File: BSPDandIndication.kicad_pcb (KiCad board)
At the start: 2 copper layers, 50 parts, among them J1 Power12, J2 Masa, J3 12VTelem, J4 Sensors, J5 12VTelem, J6 BSPD12OUT, K1 FINDER-36.11, Q1 BC817, U1 LM1117-5.0, U2 LM1117-5.0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

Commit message: Update J5 value
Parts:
- J5: value 12VTelem -> LED
- moved J4 101.0 mm to (63.5, 137.1), turned to 180 degrees
- moved J2 85.6 mm to (25.4, 132.1), turned to 90 degrees
- moved J3 59.3 mm to (25.4, 119.4), turned to 90 degrees
- moved J5 54.5 mm to (73.7, 101.6)
- moved J1 42.6 mm to (25.4, 106.7), turned to 90 degrees
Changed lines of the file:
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@@
   )
   (footprint "AK3001:AK300_1x02_P5.00mm_45-Degree" (layer "F.Cu")
-    (at 58.775 49.215)
+    (at 73.66 101.6)
     (descr "AK3001 serie terminal block")
     (tags "AK3001 serie connector")
@@
       (effects (font (size 1 1) (thickness 0.15)))
     )
-    (fp_text value "12VTelem" (at 2.5 11) (layer "F.Fab")
+    (fp_text value "LED" (at 2.5 11) (layer "F.Fab")
       (effects (font (size 1 1) (thickness 0.15)))
     )
@@
   )
   (footprint "AK3001:AK3001_1x04_P5.00mm_45-Degree" (layer "F.Cu")
-    (at 25.085 43.615)
+    (at 63.45 137.08 180)
     (descr "AK3001 serie terminal block")
     (tags "AK3001 serie connector")
@@
     (fp_line (start 17.53 8.636) (end -2.47 8.636) (layer "F.Fab") (width 0.1))
     (fp_line (start -2.47 8.636) (end -2.47 -5.5) (layer "F.Fab") (width 0.1))
-    (pad "1" thru_hole rect (at 0.03 5) (size 3 3) (drill 1.5) (layers *.Cu *.Mask)
+    (pad "1" thru_hole rect (at 0.03 5 180) (size 3 3) (drill 1.5) (layers *.Cu *.Mask)
       (net 2 "GND") (pinfunction "Pin_1") (pintype "passive"))
-    (pad "1" thru_hole rect (at 0.03 0) (size 3 3) (drill 1.5) (layers *.Cu *.Mask)
+    (pad "1" thru_hole rect (at 0.03 0 180) (size 3 3) (drill 1.5) (layers *.Cu *.Mask)
       (net 2 "GND") (pinfunction "Pin_1") (pintype "passive"))
-    (pad "2" thru_hole circle (at 5.03 5) (size 3 3) (drill 1.5) (layers *.Cu *.Mask)
+    (pad "2" thru_hole circle (at 5.03 5 180) (size 3 3) (drill 1.5) (layers *.Cu *.Mask)
       (net 16 "Brake2") (pinfunction "Pin_2") (pintype "passive"))
-    (pad "2" thru_hole circle (at 5.03 0) (size 3 3) (drill 1.5) (layers *.Cu *.Mask)
+    (pad "2" thru_hole circle (at 5.03 0 180) (size 3 3) (drill 1.5) (layers *.Cu *.Mask)
       (net 16 "Brake2") (pinfunction "Pin_2") (pintype "passive"))
-    (pad "3" thru_hole circle (at 10.03 0) (size 3 3) (drill 1.5) (layers *.Cu *.Mask)
+    (pad "3" thru_hole circle (at 10.03 0 180) (size 3 3) (drill 1.5) (layers *.Cu *.Mask)
       (net 17 "Brake1") (pinfunction "Pin_3") (pintype "passive"))
-    (pad "3" thru_hole circle (at 10.03 5) (size 3 3) (drill 1.5) (layers *.Cu *.Mask)
+    (pad "3" thru_hole circle (at 10.03 5 180) (size 3 3) (drill 1.5) (layers *.Cu *.Mask)
       (net 17 "Brake1") (pinfunction "Pin_3") (pintype "passive"))
-    (pad "4" thru_hole circle (at 15.03 5) (size 3 3) (drill 1.5) (layers *.Cu *.Mask)
+    (pad "4" thru_hole circle (at 15.03 5 180) (size 3 3) (drill 1.5) (layers *.Cu *.Mask)
       (net 18 "TPS") (pinfunction "Pin_4") (pintype "passive"))
-    (pad "4" thru_hole circle (at 15.03 0) (size 3 3) (drill 1.5) (layers *.Cu *.Mask)
+    (pad "4" thru_hole circle (at 15.03 0 180) (size 3 3) (drill 1.5) (layers *.Cu *.Mask)
       (net 18 "TPS") (pinfunction "Pin_4") (pintype "passive"))
     (model "${KICAD6_3DMODEL_DIR}/TerminalBlock_Altech.3dshapes/Altech_AK300_1x04_P5.00mm_45-Degree.wrl"
@@
   )
   (footprint "AK3001:AK300_1x02_P5.00mm_45-Degree" (layer "F.Cu")
-    (at 25.115 60.085)
+    (at 25.4 119.38 90)
     (descr "AK3001 serie terminal block")
     (tags "AK3001 serie connector")
@@
     (property "Sheetname" "")
     (attr through_hole)
-    (fp_text reference "J3" (at 0 -7.2) (layer "F.SilkS")
-      (effects (font (size 1 1) (thickness 0.15)))
-    )
-    (fp_text value "12VTelem" (at 2.5 11) (layer "F.Fab")
-      (effects (font (size 1 1) (thickness 0.15)))
-    )
-    (fp_text user "${REFERENCE}" (at 2.5 0.25) (layer "F.Fab")
+    (fp_text reference "J3" (at 0 -7.2 90) (layer "F.SilkS")
+      (effects (font (size 1 1) (thickness 0.15)))
+    )
+    (fp_text value "12VTelem" (at 2.5 11 90) (layer "F.Fab")
+      (effects (font (size 1 1) (thickness 0.15)))
+    )
+    (fp_text user "${REFERENCE}" (at 2.5 0.25 90) (layer "F.Fab")
       (effects (font (size 1 1) (thickness 0.15)))
     )
@@
     (fp_line (start 7.5 -6) (end 7.5 8.636) (layer "F.Fab") (width 0.1))
     (fp_line (start -2.5 8.636) (end -2.5 -5.5) (layer "F.Fab") (width 0.1))
-    (pad "1" thru_hole rect (at 0 0) (size 3 3) (drill 1.5) (layers *.Cu *.Mask)
+    (pad "1" thru_hole rect (at 0 0 90) (size 3 3) (drill 1.5) (layers *.Cu *.Mask)
       (net 3 "12V_Telem") (pinfunction "Pin_1") (pintype "passive"))
-    (pad "1" thru_hole rect (at 0 5) (size 3 3) (drill 1.5) (layers *.Cu *.Mask)
+    (pad "1" thru_hole rect (at 0 5 90) (size 3 3) (drill 1.5) (layers *.Cu *.Mask)
       (net 3 "12V_Telem") (pinfunction "Pin_1") (pintype "passive"))
-    (pad "2" thru_hole circle (at 5 0) (size 3 3) (drill 1.5) (layers *.Cu *.Mask)
+    (pad "2" thru_hole circle (at 5 0 90) (size 3 3) (drill 1.5) (layers *.Cu *.Mask)
       (net 3 "12V_Telem") (pinfunction "Pin_2") (pintype "passive"))
-    (pad "2" thru_hole circle (at 5 5) (size 3 3) (drill 1.5) (layers *.Cu *.Mask)
+    (pad "2" thru_hole circle (at 5 5 90) (size 3 3) (drill 1.5) (layers *.Cu *.Mask)
       (net 3 "12V_Telem") (pinfunction "Pin_2") (pintype "passive"))
     (model "${KICAD6_3DMODEL_DIR}/TerminalBlock_Altech.3dshapes/Altech_AK300_1x02_P5.00mm_45-Degree.wrl"
@@
   )
   (footprint "AK3001:AK300_1x02_P5.00mm_45-Degree" (layer "F.Cu")
-    (at 36.945 65.685)
+    (at 25.4 106.68 90)
     (descr "AK3001 serie terminal block")
     (tags "AK3001 serie connector")
@@
     (property "Sheetname" "")
     (attr through_hole)
-    (fp_text reference "J1" (at 0 -7.2) (layer "F.SilkS")
-      (effects (font (size 1 1) (thickness 0.15)))
-    )
-    (fp_text value "Power12" (at 2.5 11) (layer "F.Fab")
-      (effects (font (size 1 1) (thickness 0.15)))
-    )
-    (fp_text user "${REFERENCE}" (at 2.5 0.25) (layer "F.Fab")
+    (fp_text reference "J1" (at 0 -7.2 90) (layer "F.SilkS")
+      (effects (font (size 1 1) (thickness 0.15)))
+    )
+    (fp_text value "Power12" (at 2.5 11 90) (layer "F.Fab")
+      (effects (font (size 1 1) (thickness 0.15)))
+    )
+    (fp_text user "${REFERENCE}" (at 2.5 0.25 90) (layer "F.Fab")
       (effects (font (size 1 1) (thickness 0.15)))
     )
@@
     (fp_line (start -2 -6) (end 7.5 -6) (layer "F.Fab") (width 0.1))
     (fp_line (start 7.5 8.636) (end -2.5 8.636) (layer "F.Fab") (width 0.1))
-    (pad "1" thru_hole rect (at 0 5) (size 3 3) (drill 1.5) (layers *.Cu *.Mask)
+    (pad "1" thru_hole rect (at 0 5 90) (size 3 3) (drill 1.5) (layers *.Cu *.Mask)
       (net 13 "+12C") (pinfunction "Pin_1") (pintype "passive"))
-    (pad "1" thru_hole rect (at 0 0) (size 3 3) (drill 1.5) (layers *.Cu *.Mask)
+    (pad "1" thru_hole rect (at 0 0 90) (size 3 3) (drill 1.5) (layers *.Cu *.Mask)
       (net 13 "+12C") (pinfunction "Pin_1") (pintype "passive"))
-    (pad "2" thru_hole circle (at 5 0) (size 3 3) (drill 1.5) (layers *.Cu *.Mask)
+    (pad "2" thru_hole circle (at 5 0 90) (size 3 3) (drill 1.5) (layers *.Cu *.Mask)
       (net 13 "+12C") (pinfunction "Pin_2") (pintype "passive"))
-    (pad "2" thru_hole circle (at 5 5) (size 3 3) (drill 1.5) (layers *.Cu *.Mask)
+    (pad "2" thru_hole circle (at 5 5 90) (size 3 3) (drill 1.5) (layers *.Cu *.Mask)
       (net 13 "+12C") (pinfunction "Pin_2") (pintype "passive"))
     (model "${KICAD6_3DMODEL_DIR}/TerminalBlock_Altech.3dshapes/Altech_AK300_1x02_P5.00mm_45-Degree.wrl"
@@
   )
   (footprint "AK3001:AK300_1x02_P5.00mm_45-Degree" (layer "F.Cu")
-    (at 46.945 49.215)
+    (at 25.4 132.08 90)
     (descr "AK3001 serie terminal block")
     (tags "AK3001 serie connector")
@@
     (property "Sheetname" "")
     (attr through_hole)
-    (fp_text reference "J2" (at 0 -7.2) (layer "F.SilkS")
-      (effects (font (size 1 1) (thickness 0.15)))
-    )
-    (fp_text value "Masa" (at 2.5 11) (layer "F.Fab")
-      (effects (font (size 1 1) (thickness 0.15)))
-    )
-    (fp_text user "${REFERENCE}" (at 2.5 0.25) (layer "F.Fab")
+    (fp_text reference "J2" (at 0 -7.2 90) (layer "F.SilkS")
+      (effects (font (size 1 1) (thickness 0.15)))
+    )
+    (fp_text value "Masa" (at 2.5 11 90) (layer "F.Fab")
+      (effects (font (size 1 1) (thickness 0.15)))
+    )
+    (fp_text user "${REFERENCE}" (at 2.5 0.25 90) (layer "F.Fab")
       (effects (font (size 1 1) (thickness 0.15)))
     )
@@
     (fp_line (start -2.5 8.636) (end -2.5 -5.5) (layer "F.Fab") (width 0.1))
     (fp_line (start 7.5 8.636) (end -2.5 8.636) (layer "F.Fab") (width 0.1))
-    (pad "1" thru_hole rect (at 0 5) (size 3 3) (drill 1.5) (layers *.Cu *.Mask)
+    (pad "1" thru_hole rect (at 0 5 90) (size 3 3) (drill 1.5) (layers *.Cu *.Mask)
       (net 2 "GND") (pinfunction "Pin_1") (pintype "passive"))
-    (pad "1" thru_hole rect (at 0 0) (size 3 3) (drill 1.5) (layers *.Cu *.Mask)
+    (pad "1" thru_hole rect (at 0 0 90) (size 3 3) (drill 1.5) (layers *.Cu *.Mask)
       (net 2 "GND") (pinfunction "Pin_1") (pintype "passive"))
-    (pad "2" thru_hole circle (at 5 5) (size 3 3) (drill 1.5) (layers *.Cu *.Mask)
+    (pad "2" thru_hole circle (at 5 5 90) (size 3 3) (drill 1.5) (layers *.Cu *.Mask)
       (net 2 "GND") (pinfunction "Pin_2") (pintype "passive"))
-    (pad "2" thru_hole circle (at 5 0) (size 3 3) (drill 1.5) (layers *.Cu *.Mask)
+    (pad "2" thru_hole circle (at 5 0 90) (size 3 3) (drill 1.5) (layers *.Cu *.Mask)
       (net 2 "GND") (pinfunction "Pin_2") (pintype "passive"))
     (model "${KICAD6_3DMODEL_DIR}/TerminalBlock_Altech.3dshapes/Altech_AK300_1x02_P5.00mm_45-Degree.wrl"

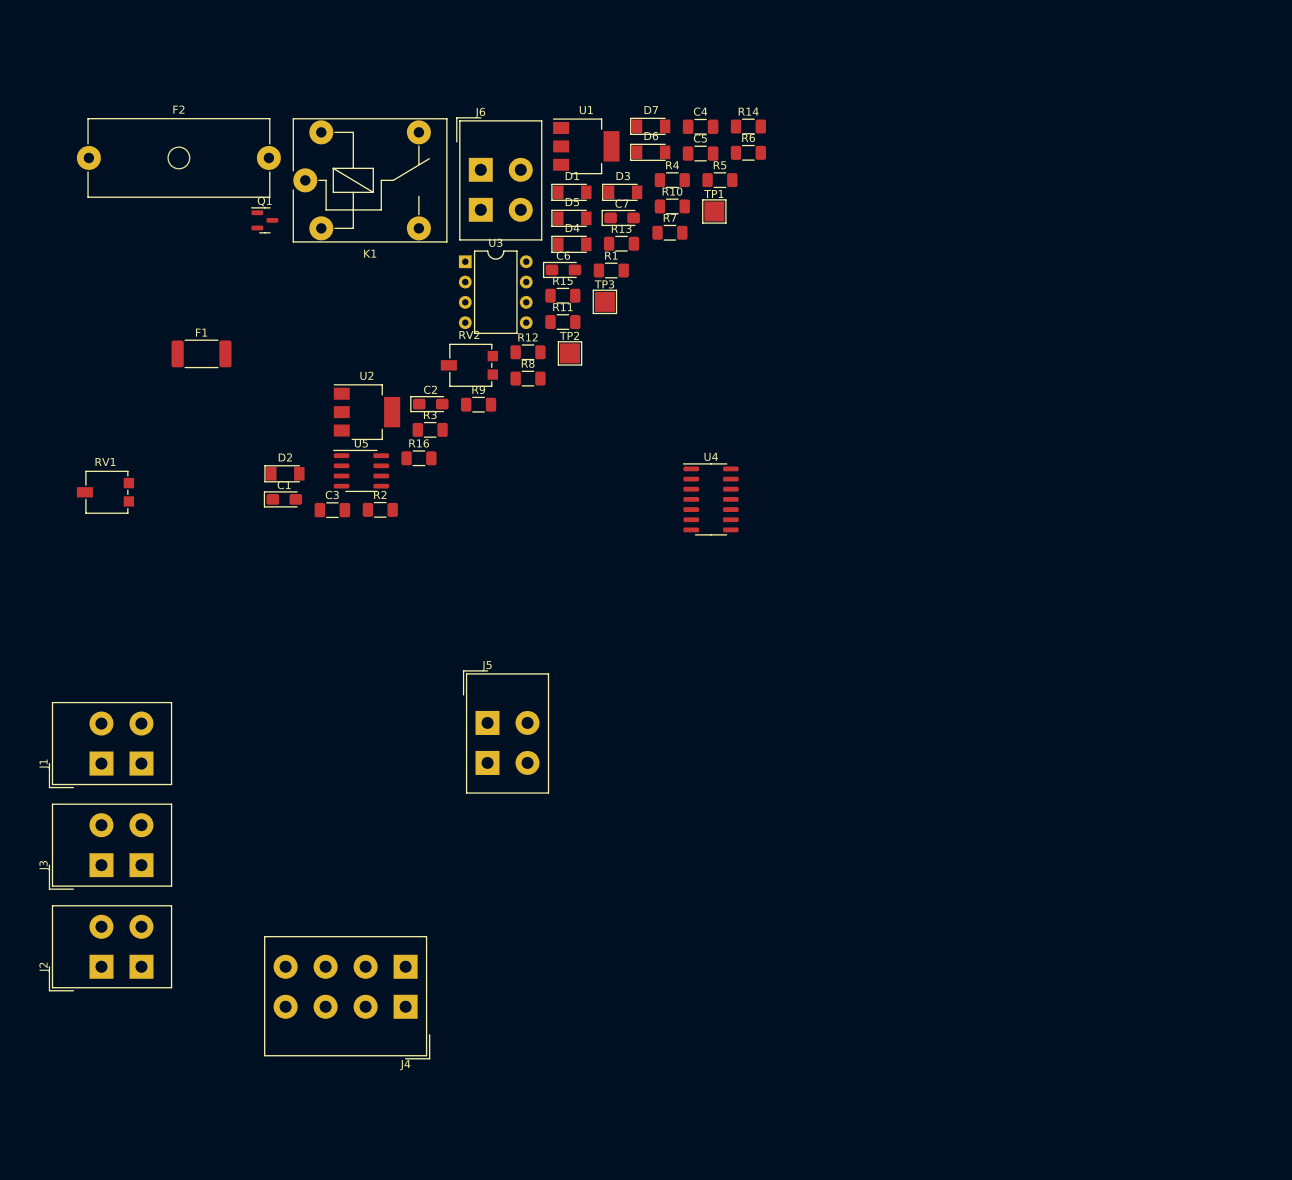
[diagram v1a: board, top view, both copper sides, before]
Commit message: Return safety pin (to recognize when safety fail)
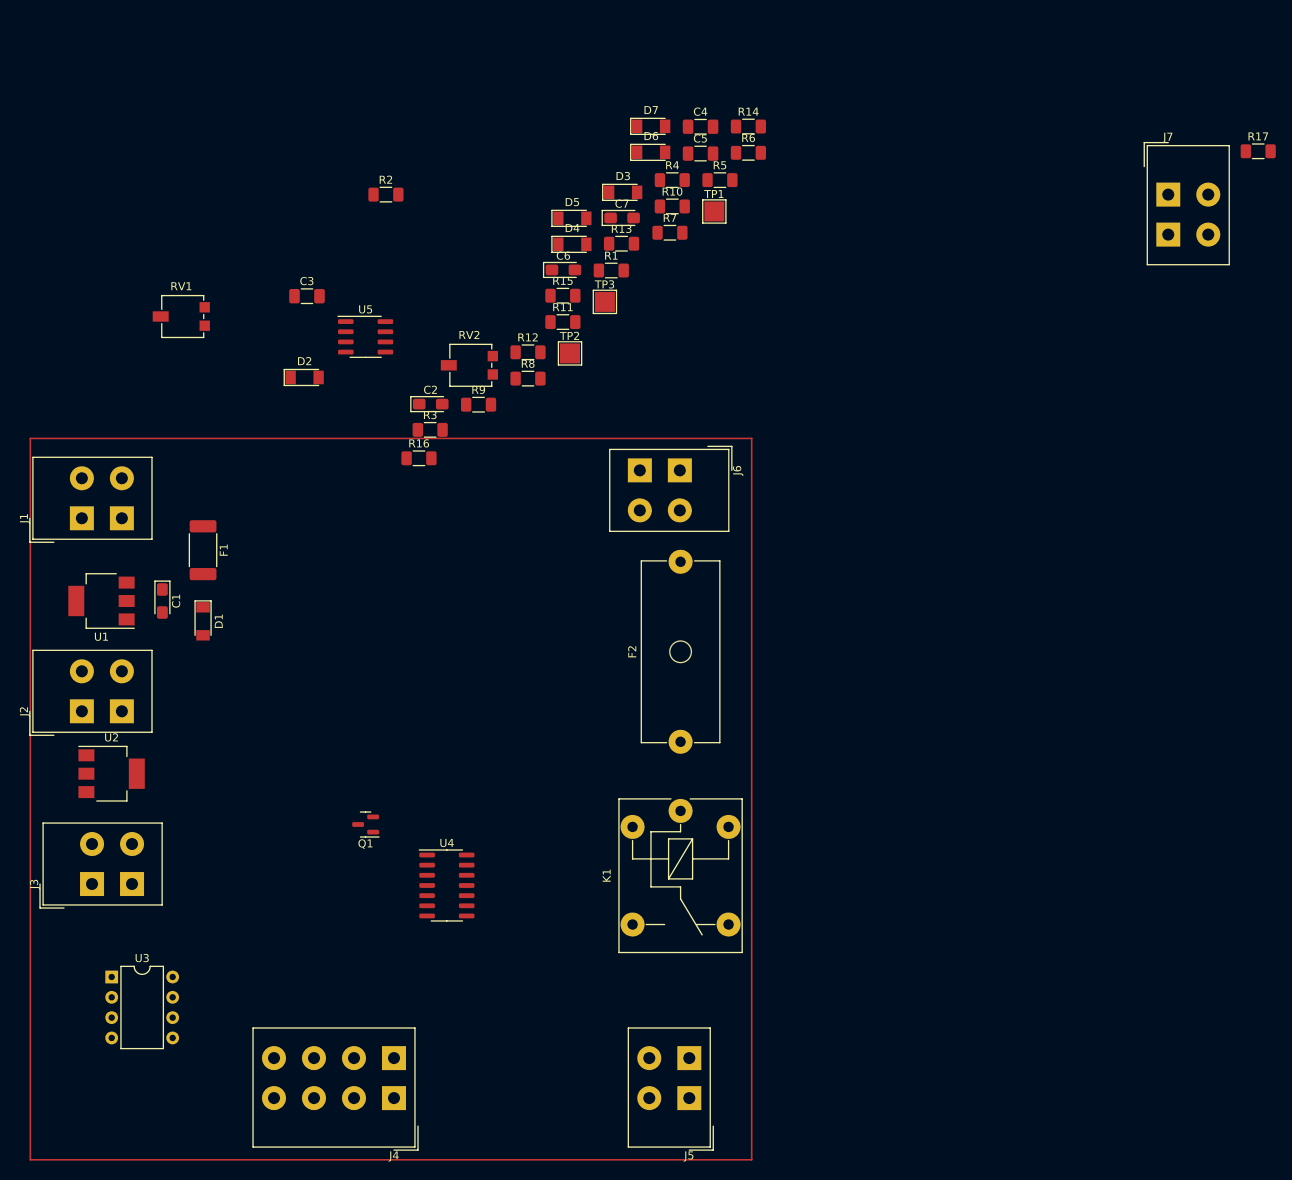
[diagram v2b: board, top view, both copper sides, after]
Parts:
- added J7: SafetyReturn, AK3001:AK300_1x02_P5.00mm_45-Degree, F.Cu at (158.8, 35.6)
- added R17: 4k7, Resistor_SMD:R_1206_3216Metric_Pad1.30x1.75mm_HandSolder, F.Cu at (170.0, 30.1)
- J1: value Power12 -> SafetyIN
- moved F2 103.9 mm to (97.8, 104.0), turned to 90 degrees
- moved U3 99.7 mm to (26.7, 133.4)
- moved K1 91.7 mm to (97.8, 112.6), turned to -90 degrees
- moved U1 83.1 mm to (25.4, 86.4), turned to 180 degrees
- moved Q1 76.6 mm to (58.4, 114.3), turned to 180 degrees
- moved D1 70.8 mm to (38.1, 88.9), turned to -90 degrees
- moved U4 58.5 mm to (68.6, 121.9)
- moved U2 55.3 mm to (26.7, 108.0)
- moved J5 53.2 mm to (98.9, 148.5), turned to 180 degrees
- moved J6 45.1 mm to (97.7, 70.0), turned to -90 degrees
- moved R2 39.4 mm to (61.0, 35.6)
- moved J2 32.0 mm to (23.0, 100.1)
- moved J1 30.8 mm to (23.0, 76.0)
- moved C3 26.9 mm to (51.1, 48.3)
- moved F1 24.5 mm to (38.1, 80.0), turned to -90 degrees
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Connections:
- R7 pad 1: +5V -> Net-(U3-Pad5)
- U3 pad 5: Net-(R7-Pad2) -> Net-(U3-Pad5)

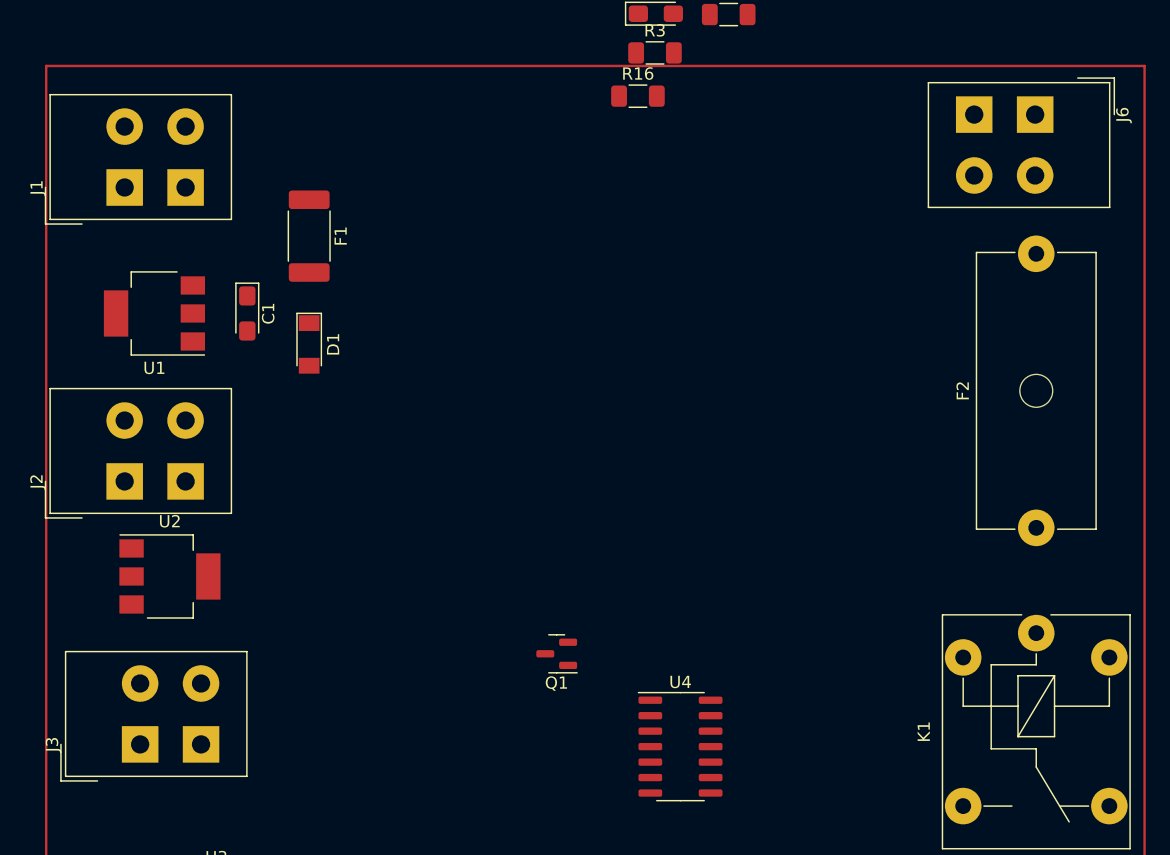
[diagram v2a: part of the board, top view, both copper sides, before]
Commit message: Only one fuse needed
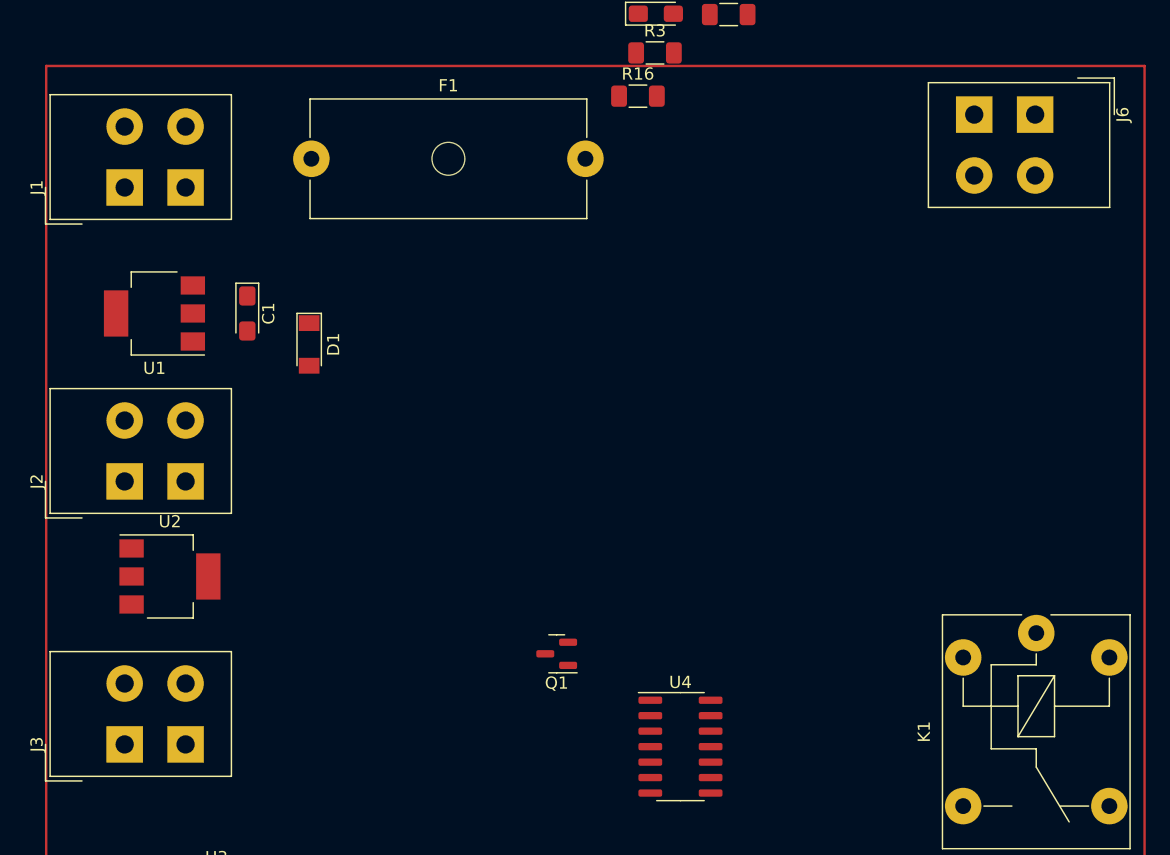
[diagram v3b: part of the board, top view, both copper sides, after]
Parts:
- removed F2: 5A, Fuse:Fuseholder_Cylinder-5x20mm_Schurter_0031_8201_Horizontal_Open
- F1: value 2A -> 5A; footprint Fuse:Fuse_2512_6332Metric_Pad1.52x3.35mm_HandSolder -> Fuse:Fuseholder_Cylinder-5x20mm_Schurter_0031_8201_Horizontal_Open
- moved F1 6.35 mm to (38.3, 73.7), turned to 0 degrees
- moved J3 1.27 mm to (23.0, 121.7)
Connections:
- J6 pad 1: Net-(F2-Pad2) -> Net-(K1-Pad11)
- J6 pad 2: Net-(F2-Pad2) -> Net-(K1-Pad11)
- K1 pad 11: Net-(F2-Pad1) -> Net-(K1-Pad11)
